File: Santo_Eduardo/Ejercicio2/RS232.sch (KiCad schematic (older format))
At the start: 7 parts, among them J1 DB9, U2 MAX232

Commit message: Realizado el Electrical Rule Check. Corregidos Errores Se agregó campo Digikey/Mouser en todos los componentes Se modificó Digikey/Mouser en U1 y U2
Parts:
- U2: Digikey/Mouser (none) -> 1016-1803-1-ND
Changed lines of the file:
@@
 F 2 "" H 5250 3450 60  0000 C CNN
 F 3 "" H 5250 3450 60  0000 C CNN
+F 4 "1016-1803-1-ND" H 5250 3250 60  0001 C CNN "Digikey/Mouser"
 	1    5250 3250
 	1    0    0    -1
@@
 $EndComp
 Connection ~ 6250 2550
-Wire Wire Line
-	5250 2450 5250 2175
-Wire Wire Line
-	5250 2175 5850 2175
 $Comp
 L +3.3V #PWR012
 U 1 1 565E8D43
-P 5250 2175
-F 0 "#PWR012" H 5250 2135 30  0001 C CNN
-F 1 "+3.3V" H 5250 2285 30  0000 C CNN
-F 2 "" H 5250 2175 60  0000 C CNN
-F 3 "" H 5250 2175 60  0000 C CNN
-	1    5250 2175
+P 5250 1825
+F 0 "#PWR012" H 5250 1785 30  0001 C CNN
+F 1 "+3.3V" H 5250 1935 30  0000 C CNN
+F 2 "" H 5250 1825 60  0000 C CNN
+F 3 "" H 5250 1825 60  0000 C CNN
+	1    5250 1825
 	1    0    0    -1
 $EndComp
+$Comp
+L +3.3V #PWR013
+U 1 1 565EA809
+P 5850 2050
+F 0 "#PWR013" H 5850 2010 30  0001 C CNN
+F 1 "+3.3V" H 5850 2160 30  0000 C CNN
+F 2 "" H 5850 2050 60  0000 C CNN
+F 3 "" H 5850 2050 60  0000 C CNN
+	1    5850 2050
+	1    0    0    -1
+$EndComp
+Wire Wire Line
+	5850 2050 5850 2175
+Wire Wire Line
+	5250 1825 5250 2450
 $EndSCHEMATC

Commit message: Added footprint library Assigned Foot-Symbol updated netlist and BOM
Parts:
- C2, C3, C4, C5, C6: footprint (none) -> Ejercicio2:C_0603_HandSoldering
- J1: footprint (none) -> Ejercicio2:DB9_F_TH
- U2: footprint (none) -> Ejercicio2:SP3232ECN-SOIC16N
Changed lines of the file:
@@
 F 0 "C2" V 4150 2625 40  0000 L CNN
 F 1 "100nF" V 4225 2550 40  0000 L CNN
-F 2 "" H 4388 2600 30  0000 C CNN
+F 2 "Ejercicio2:C_0603_HandSoldering" H 4388 2600 30  0001 C CNN
 F 3 "" H 4350 2750 60  0000 C CNN
 	1    4350 2750
@@
 F 0 "C3" V 4200 2925 40  0000 L CNN
 F 1 "100nF" V 4300 2775 40  0000 L CNN
-F 2 "" H 4388 2900 30  0000 C CNN
+F 2 "Ejercicio2:C_0603_HandSoldering" H 4388 2900 30  0001 C CNN
 F 3 "" H 4350 3050 60  0000 C CNN
 	1    4350 3050
@@
 F 0 "U2" H 4750 4250 60  0000 C CNN
 F 1 "MAX232" H 4750 4150 60  0000 C CNN
-F 2 "" H 5250 3450 60  0000 C CNN
+F 2 "Ejercicio2:SP3232ECN-SOIC16N" H 5250 3450 60  0001 C CNN
 F 3 "" H 5250 3450 60  0000 C CNN
 F 4 "1016-1803-1-ND" H 5250 3250 60  0001 C CNN "Digikey/Mouser"
@@
 F 0 "J1" H 8300 3725 70  0000 C CNN
 F 1 "DB9" H 8300 2625 70  0000 C CNN
-F 2 "" H 8300 3175 60  0000 C CNN
+F 2 "Ejercicio2:DB9_F_TH" H 8300 3175 60  0001 C CNN
 F 3 "" H 8300 3175 60  0000 C CNN
 	1    8300 3175
@@
 F 0 "C5" V 5850 2425 40  0000 L CNN
 F 1 "100nF" V 5925 2350 40  0000 L CNN
-F 2 "" H 6088 2400 30  0000 C CNN
+F 2 "Ejercicio2:C_0603_HandSoldering" H 6088 2400 30  0001 C CNN
 F 3 "" H 6050 2550 60  0000 C CNN
 	1    6050 2550
@@
 F 0 "C6" V 5850 2875 40  0000 L CNN
 F 1 "100nF" V 5925 2800 40  0000 L CNN
-F 2 "" H 6088 2850 30  0000 C CNN
+F 2 "Ejercicio2:C_0603_HandSoldering" H 6088 2850 30  0001 C CNN
 F 3 "" H 6050 3000 60  0000 C CNN
 	1    6050 3000
@@
 F 0 "C4" V 5850 2050 40  0000 L CNN
 F 1 "100nF" V 5925 1975 40  0000 L CNN
-F 2 "" H 6088 2025 30  0000 C CNN
+F 2 "Ejercicio2:C_0603_HandSoldering" H 6088 2025 30  0001 C CNN
 F 3 "" H 6050 2175 60  0000 C CNN
 	1    6050 2175

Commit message: Cambiados footprints Revisando placement en PCB
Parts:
- C2, C3, C4, C5, C6: footprint Ejercicio2:C_0603_HandSoldering -> Ejercicio2:1206
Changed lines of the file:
@@
 F 0 "C2" V 4150 2625 40  0000 L CNN
 F 1 "100nF" V 4225 2550 40  0000 L CNN
-F 2 "Ejercicio2:C_0603_HandSoldering" H 4388 2600 30  0001 C CNN
+F 2 "Ejercicio2:1206" H 4388 2600 30  0001 C CNN
 F 3 "" H 4350 2750 60  0000 C CNN
 	1    4350 2750
@@
 F 0 "C3" V 4200 2925 40  0000 L CNN
 F 1 "100nF" V 4300 2775 40  0000 L CNN
-F 2 "Ejercicio2:C_0603_HandSoldering" H 4388 2900 30  0001 C CNN
+F 2 "Ejercicio2:1206" H 4388 2900 30  0001 C CNN
 F 3 "" H 4350 3050 60  0000 C CNN
 	1    4350 3050
@@
 F 0 "C5" V 5850 2425 40  0000 L CNN
 F 1 "100nF" V 5925 2350 40  0000 L CNN
-F 2 "Ejercicio2:C_0603_HandSoldering" H 6088 2400 30  0001 C CNN
+F 2 "Ejercicio2:1206" H 6088 2400 30  0001 C CNN
 F 3 "" H 6050 2550 60  0000 C CNN
 	1    6050 2550
@@
 F 0 "C6" V 5850 2875 40  0000 L CNN
 F 1 "100nF" V 5925 2800 40  0000 L CNN
-F 2 "Ejercicio2:C_0603_HandSoldering" H 6088 2850 30  0001 C CNN
+F 2 "Ejercicio2:1206" H 6088 2850 30  0001 C CNN
 F 3 "" H 6050 3000 60  0000 C CNN
 	1    6050 3000
@@
 F 0 "C4" V 5850 2050 40  0000 L CNN
 F 1 "100nF" V 5925 1975 40  0000 L CNN
-F 2 "Ejercicio2:C_0603_HandSoldering" H 6088 2025 30  0001 C CNN
+F 2 "Ejercicio2:1206" H 6088 2025 30  0001 C CNN
 F 3 "" H 6050 2175 60  0000 C CNN
 	1    6050 2175

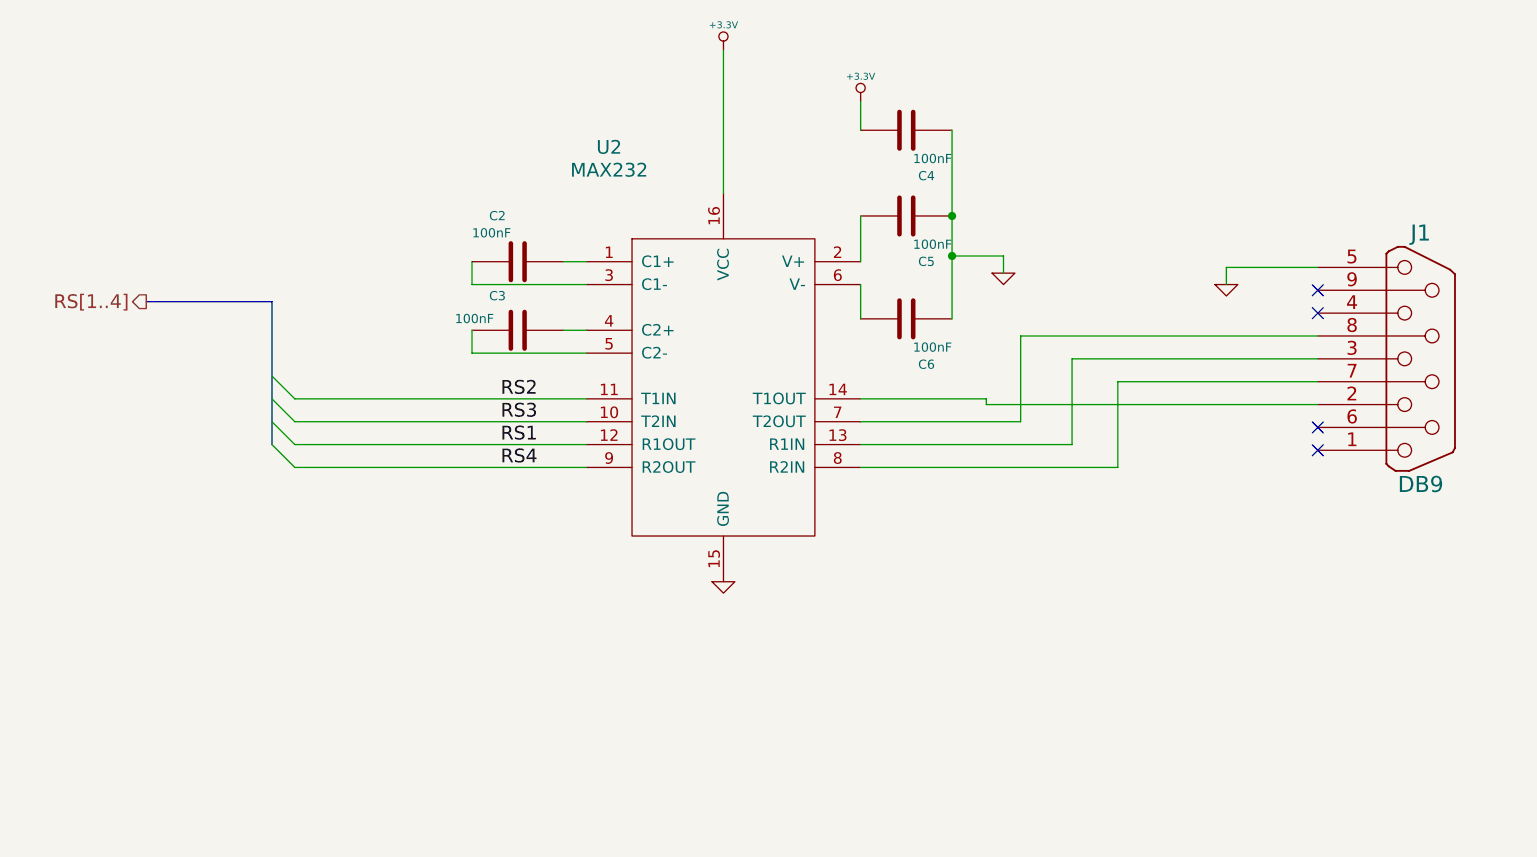
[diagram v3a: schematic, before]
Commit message: Added GND planes
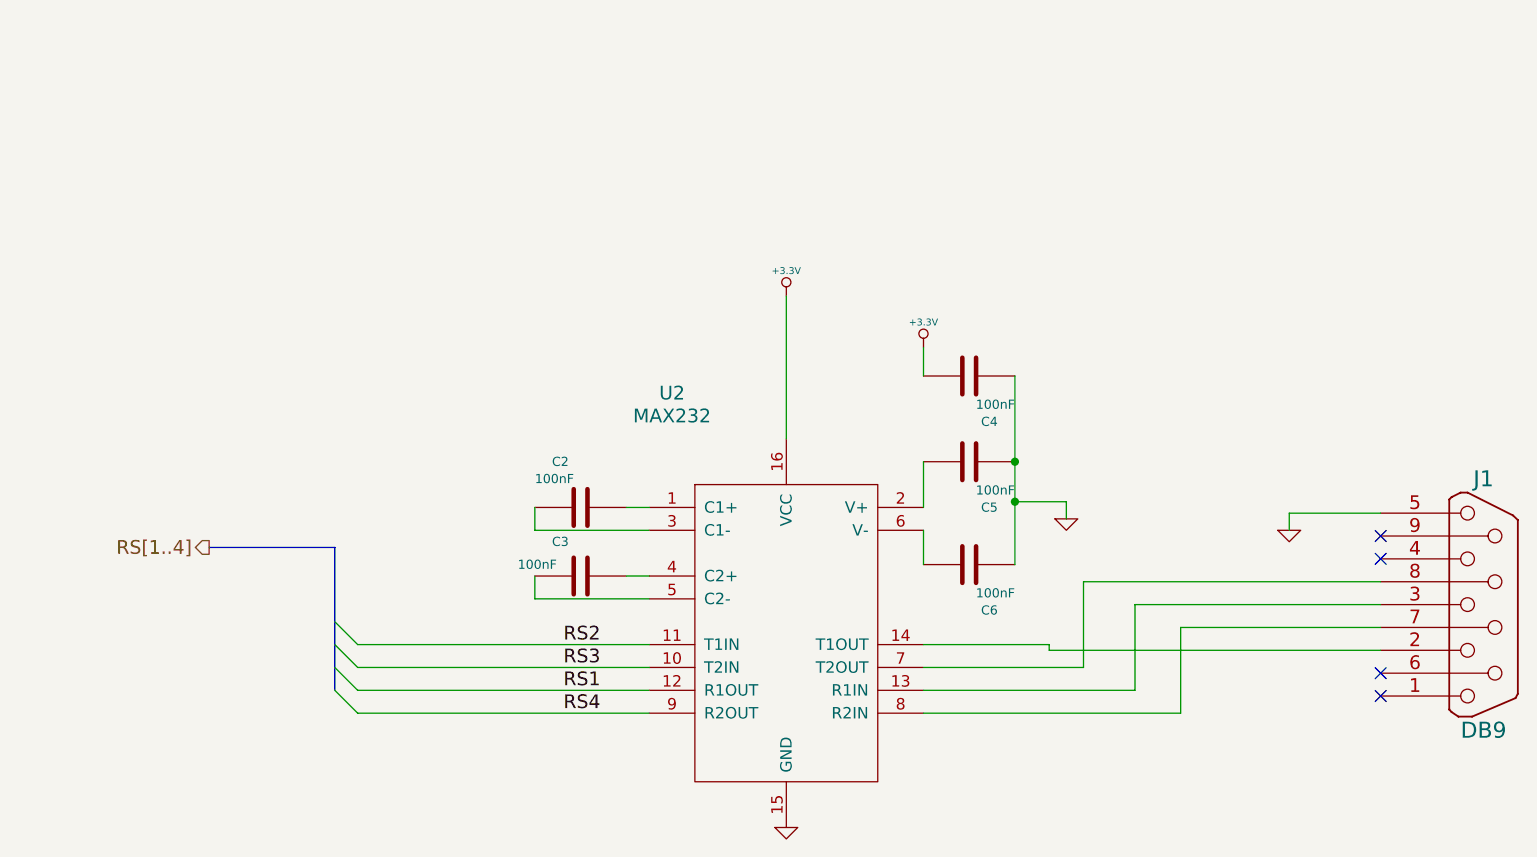
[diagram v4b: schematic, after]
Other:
- moved on the sheet: C2, C3, C4, C5, C6, J1, U2
